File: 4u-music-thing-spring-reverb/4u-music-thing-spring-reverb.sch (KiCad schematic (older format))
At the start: 42 parts, among them J1 IN1, J2 IN2, J3 REV_RETURN, J4 OUT, J5 Conn_01x04_Male, J6 REV_SEND, J7 CTRL_BOARD_HEADER, J8 MAIN_BOARD_HEADER, U1 TL072, U2 NE5532

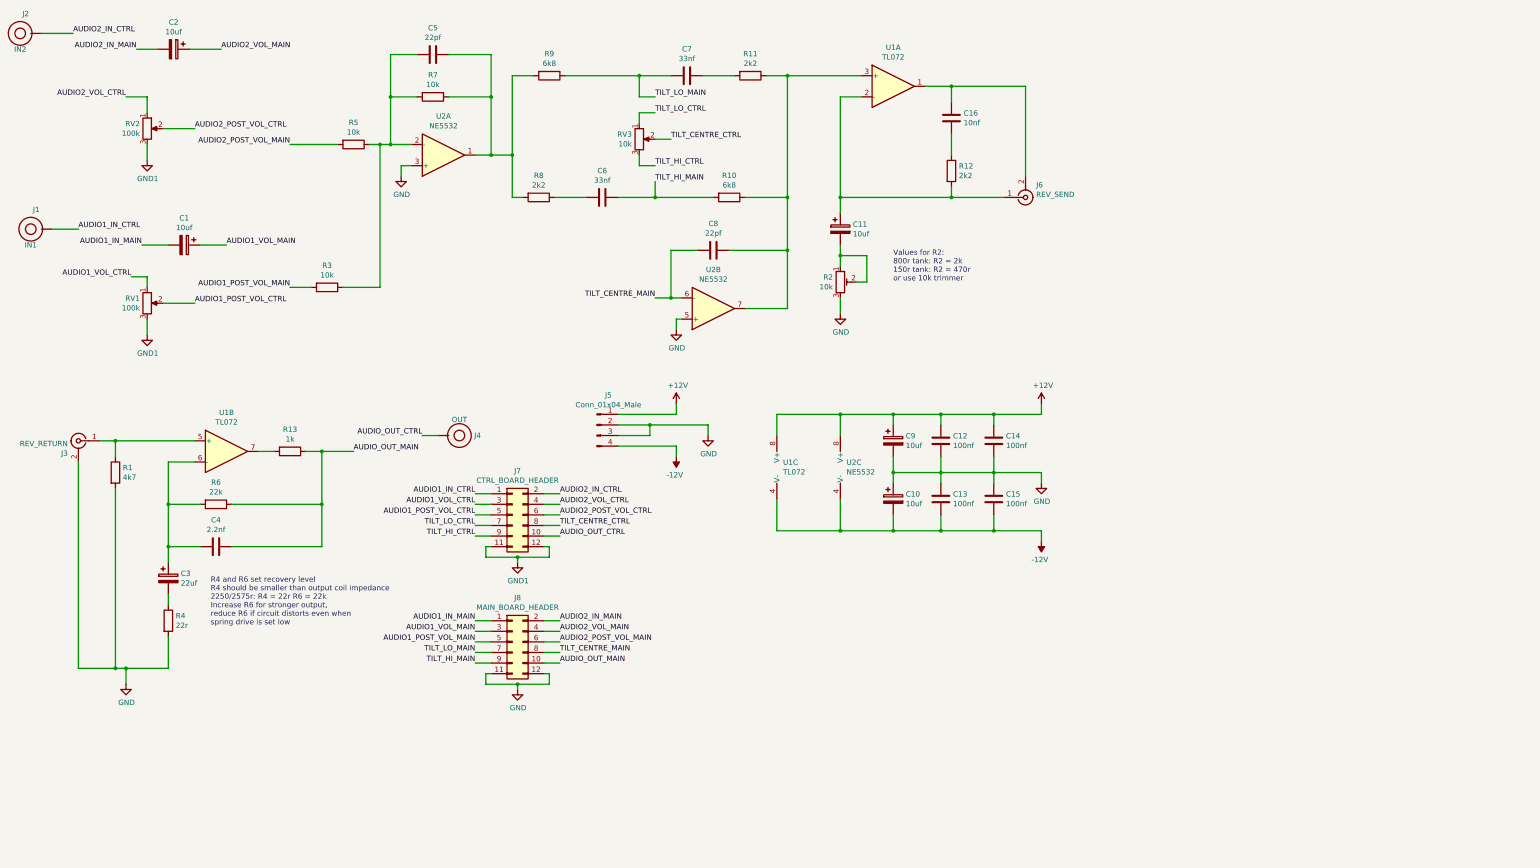
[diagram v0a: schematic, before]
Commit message: Updated version of music thing spring reverb
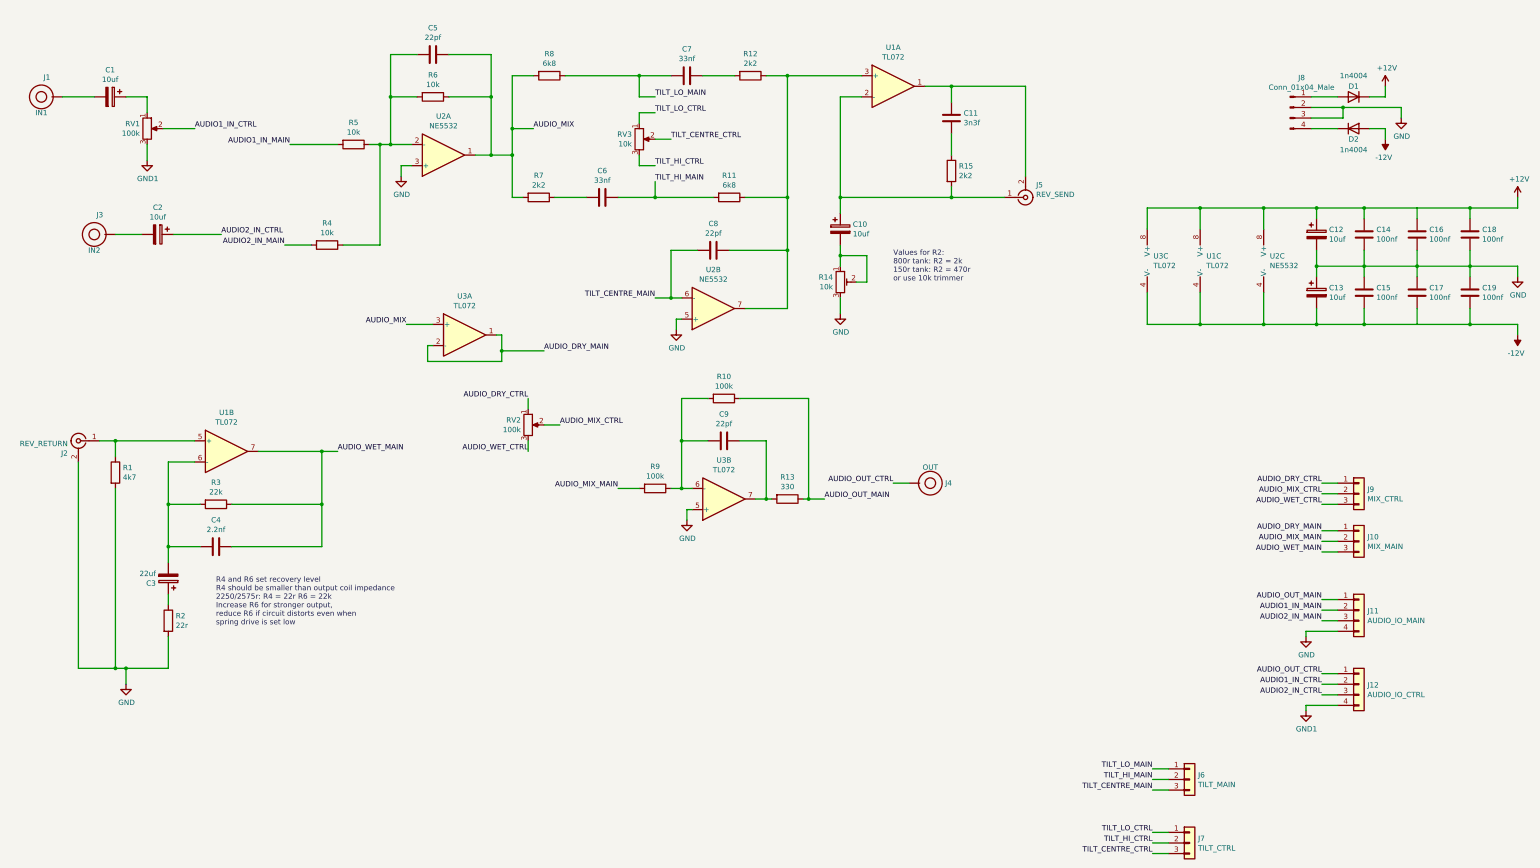
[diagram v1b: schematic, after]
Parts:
- removed J7: CTRL_BOARD_HEADER, Connector_PinHeader_2.54mm:PinHeader_2x06_P2.54mm_Vertical, symbol Connector_Generic:Conn_02x06_Odd_Even
- removed J8: MAIN_BOARD_HEADER, Connector_PinSocket_2.54mm:PinSocket_2x06_P2.54mm_Vertical, symbol Connector_Generic:Conn_02x06_Odd_Even
- removed RV1: 100k, Potentiometer_THT:Potentiometer_Alpha_RD901F-40-00D_Single_Vertical, symbol Device:R_POT
- added C14, C15: 100nf, Capacitor_THT:C_Rect_L7.0mm_W2.5mm_P5.00mm, symbol Device:C
- added C9: 22pf, Capacitor_THT:C_Rect_L7.0mm_W2.5mm_P5.00mm, symbol Device:C
- added D1, D2: 1n4004, rumblesan-footprints:Diode_THT_P7.62mm_Horizontal, symbol Device:D
- added J10: MIX_MAIN, Connector_PinSocket_2.54mm:PinSocket_1x03_P2.54mm_Vertical, symbol Connector_Generic:Conn_01x03
- added J11: AUDIO_IO_MAIN, Connector_PinSocket_2.54mm:PinSocket_1x04_P2.54mm_Vertical, symbol Connector_Generic:Conn_01x04
- added J12: AUDIO_IO_CTRL, Connector_PinHeader_2.54mm:PinHeader_1x04_P2.54mm_Vertical, symbol Connector_Generic:Conn_01x04
- added J6: TILT_MAIN, Connector_PinSocket_2.54mm:PinSocket_1x03_P2.54mm_Vertical, symbol Connector_Generic:Conn_01x03
- added J7: TILT_CTRL, Connector_PinHeader_2.54mm:PinHeader_1x03_P2.54mm_Vertical, symbol Connector_Generic:Conn_01x03
- added J9: MIX_CTRL, Connector_PinHeader_2.54mm:PinHeader_1x03_P2.54mm_Vertical, symbol Connector_Generic:Conn_01x03
- added R10, R9: 100k, rumblesan-footprints:Resistor_THT_L6.3mm_D2.5mm_P10.16mm_Horizontal, symbol Device:R
- added RV2: 100k, Potentiometer_THT:Potentiometer_Alpha_RD901F-40-00D_Single_Vertical, symbol Device:R_POT
- added U3: TL072, Package_DIP:DIP-8_W7.62mm_Socket, symbol Amplifier_Operational:TL072
- C11: renamed from C16; value 10nf -> 3n3f
- J1: renamed from J2; value IN2 -> IN1
- J3: renamed from J1; value IN1 -> IN2
- R13: value 1k -> 330
- renumbered C2 to C1, C11 to C10, C9 to C12, C10 to C13, C12 to C16, C13 to C17, C14 to C18, C15 to C19, C1 to C2, J3 to J2, J6 to J5, J5 to J8, R10 to R11, R11 to R12, R2 to R14, R12 to R15, R4 to R2, R6 to R3, R3 to R4, R7 to R6, R8 to R7, R9 to R8, RV2 to RV1
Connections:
- net AUDIO1_POST_VOL_MAIN is gone; now on net AUDIO2_IN_MAIN: R4.2
- net AUDIO1_VOL_MAIN is gone; now on net AUDIO2_IN_CTRL: C2.1
- net AUDIO2_POST_VOL_CTRL is gone; now on net AUDIO1_IN_CTRL: RV1.2
- net AUDIO2_POST_VOL_MAIN is gone; now on net AUDIO1_IN_MAIN: R5.2
- net AUDIO2_VOL_MAIN is gone; now on an unnamed net: C1.1
- net +12V: now also C14.1, D1.1 (K), U3.8 (V+); no longer J8.1 (Pin_1)
- net -12V: now also C15.2, D2.2 (A), U3.4 (V-); no longer J8.4 (Pin_4)
- net AUDIO1_IN_CTRL: now also J12.2 (Pin_2); no longer J3.1
- net AUDIO1_IN_MAIN: now also J11.2 (Pin_2); no longer C2.2
- net AUDIO2_IN_CTRL: now also J12.3 (Pin_3); no longer J1.1
- net AUDIO2_IN_MAIN: now also J11.3 (Pin_3); no longer C1.2
- net AUDIO_OUT_CTRL: now also J12.1 (Pin_1)
- net AUDIO_OUT_MAIN: now also J11.1 (Pin_1), R10.1; no longer C4.1, R3.1
- net GND: now also C14.2, C15.1, J11.4 (Pin_4), U3.5 (+)
- net GND1: now also J12.4 (Pin_4)
- net TILT_CENTRE_CTRL: now also J7.3 (Pin_3)
- net TILT_CENTRE_MAIN: now also J6.3 (Pin_3)
- net TILT_HI_CTRL: now also J7.2 (Pin_2)
- net TILT_HI_MAIN: now also J6.2 (Pin_2)
- net TILT_LO_CTRL: now also J7.1 (Pin_1)
- net TILT_LO_MAIN: now also J6.1 (Pin_1)
- net AUDIO_MIX: now reaches C5.1, R6.1, R7.2, R8.2, U2.1
- net AUDIO_MIX: now also U3.3 (+)
- net at C4.2, R3.2, U1.6 (-): now also C3.2; no longer C3.1
- net at R13.2: now also C9.1, U3.7; no longer U1.7
- net at R2.1: now also C3.1; no longer C3.2
- net AUDIO2_VOL_CTRL: no longer names the net of RV1.1
- new net: C1.2, J1.1
- new net: C2.2, J3.1
- new net: D1.2 (A), J8.1 (Pin_1)
- new net: D2.1 (K), J8.4 (Pin_4)
- new net: C9.2, R10.2, R9.1, U3.6 (-)
- new net AUDIO_DRY_CTRL: J9.1 (Pin_1), RV2.1
- new net AUDIO_DRY_MAIN: J10.1 (Pin_1), U3.1, U3.2 (-)
- new net AUDIO_MIX_CTRL: J9.2 (Pin_2), RV2.2
- new net AUDIO_MIX_MAIN: J10.2 (Pin_2), R9.2
- new net AUDIO_WET_CTRL: J9.3 (Pin_3), RV2.3
- new net AUDIO_WET_MAIN: C4.1, J10.3 (Pin_3), R3.1, U1.7
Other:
- moved on the sheet: C1, C12, C13, C16, C17, C18, C19, C2, J1, J3, J4, J8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

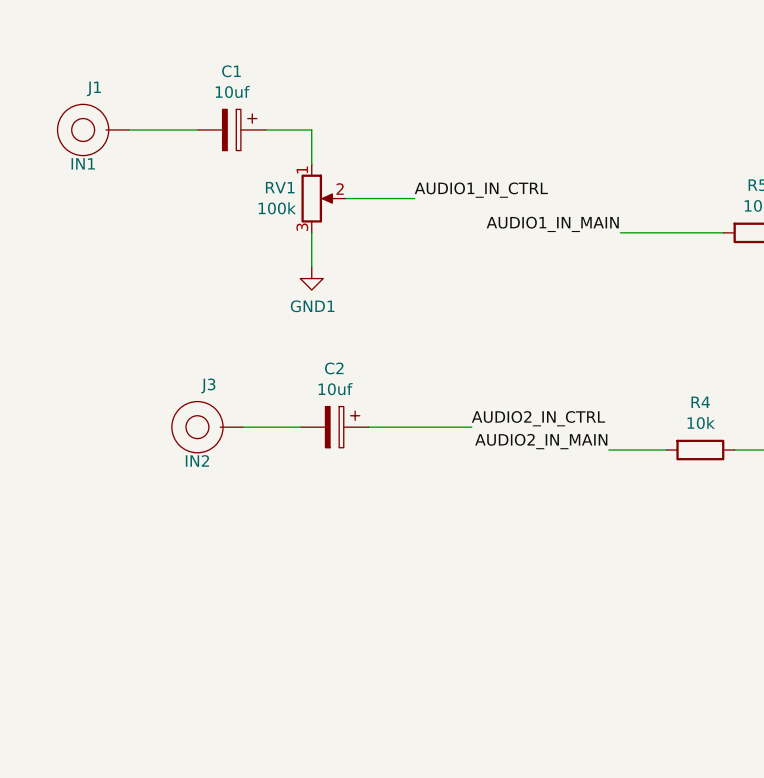
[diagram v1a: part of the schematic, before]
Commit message: Updating spring reverb to rev3
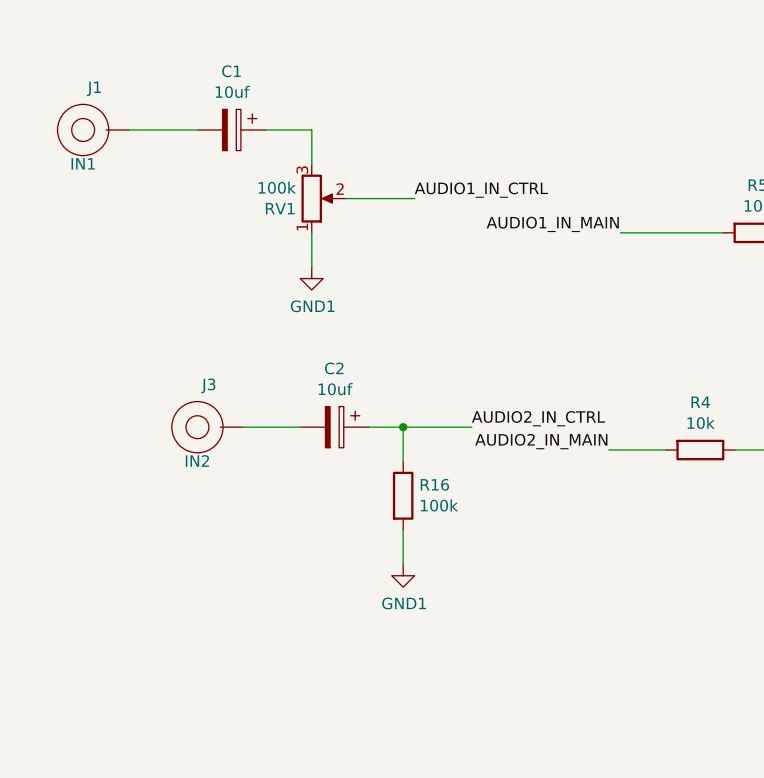
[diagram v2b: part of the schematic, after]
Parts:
- added R16: 100k, rumblesan-footprints:Resistor_THT_L6.3mm_D2.5mm_P10.16mm_Horizontal, symbol Device:R
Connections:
- net AUDIO2_IN_CTRL: now also R16.1
- net GND1: now also RV1.1, R16.2; no longer RV1.3
- net at C1.1: now also RV1.3; no longer RV1.1
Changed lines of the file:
@@
 encoding utf-8
 Sheet 1 1
-Title ""
-Date ""
-Rev "v02"
+Title "4U Spring Reverb"
+Date "2021-08-10"
+Rev "v03"
 Comp ""
-Comment1 ""
+Comment1 "Based on the Music Thing spring reverb"
 Comment2 "creativecommons.org/licenses/by/4.0/"
 Comment3 "License: CC BY 4.0"
@@
 	1    0    0    -1
 $EndComp
-Wire Wire Line
-	2150 2050 2450 2050
 Wire Wire Line
 	2000 2200 2000 2350
@@
 	7650 3750 8050 3750
 $Comp
-L Device:R_POT RV1
-U 1 1 60F258F1
-P 2000 2050
-F 0 "RV1" H 1931 2096 50  0000 R CNN
-F 1 "100k" H 1931 2005 50  0000 R CNN
-F 2 "Potentiometer_THT:Potentiometer_Alpha_RD901F-40-00D_Single_Vertical" H 2000 2050 50  0001 C CNN
-F 3 "~" H 2000 2050 50  0001 C CNN
-	1    2000 2050
-	1    0    0    -1
-$EndComp
-$Comp
 L Amplifier_Operational:NE5532 U2
 U 1 1 60F4EFDC
@@
 Wire Wire Line
 	2000 1750 1800 1750
-Wire Wire Line
-	2000 1750 2000 1900
 Wire Wire Line
 	3800 2200 3350 2200
@@
 Text Label 3350 2200 2    50   ~ 0
 AUDIO1_IN_MAIN
-Text Label 2450 2050 0    50   ~ 0
-AUDIO1_IN_CTRL
-Wire Wire Line
-	2250 3050 2700 3050
+Wire Wire Line
+	2250 3050 2400 3050
 Wire Wire Line
 	4200 2200 4300 2200
@@
 	1    0    0    -1
 $EndComp
+Text Label 2450 2050 0    50   ~ 0
+AUDIO1_IN_CTRL
+Wire Wire Line
+	2000 1750 2000 1900
+$Comp
+L Device:R_POT RV1
+U 1 1 60F258F1
+P 2000 2050
+F 0 "RV1" H 1931 2096 50  0000 R CNN
+F 1 "100k" H 1931 2005 50  0000 R CNN
+F 2 "Potentiometer_THT:Potentiometer_Alpha_RD901F-40-00D_Single_Vertical" H 2000 2050 50  0001 C CNN
+F 3 "~" H 2000 2050 50  0001 C CNN
+	1    2000 2050
+	1    0    0    1
+$EndComp
+Wire Wire Line
+	2150 2050 2450 2050
+$Comp
+L Device:R R16
+U 1 1 612196CB
+P 2400 3350
+F 0 "R16" H 2470 3396 50  0000 L CNN
+F 1 "100k" H 2470 3305 50  0000 L CNN
+F 2 "rumblesan-footprints:Resistor_THT_L6.3mm_D2.5mm_P10.16mm_Horizontal" V 2330 3350 50  0001 C CNN
+F 3 "~" H 2400 3350 50  0001 C CNN
+	1    2400 3350
+	1    0    0    -1
+$EndComp
+$Comp
+L power:GND1 #PWR015
+U 1 1 61219B73
+P 2400 3650
+F 0 "#PWR015" H 2400 3400 50  0001 C CNN
+F 1 "GND1" H 2405 3477 50  0000 C CNN
+F 2 "" H 2400 3650 50  0001 C CNN
+F 3 "" H 2400 3650 50  0001 C CNN
+	1    2400 3650
+	1    0    0    -1
+$EndComp
+Wire Wire Line
+	2400 3200 2400 3050
+Connection ~ 2400 3050
+Wire Wire Line
+	2400 3050 2700 3050
+Wire Wire Line
+	2400 3650 2400 3500
 $EndSCHEMATC
